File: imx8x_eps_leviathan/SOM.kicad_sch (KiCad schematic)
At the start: 2 parts, among them J10 BTH-070-02-L-D-A, J9 BTH-070-02-L-D-A (A to B)

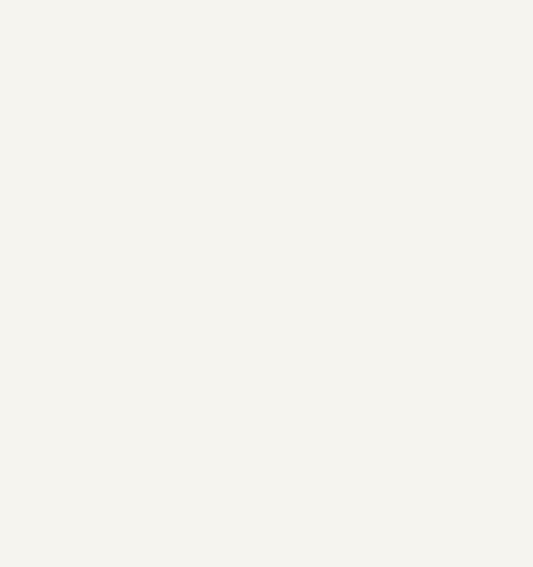
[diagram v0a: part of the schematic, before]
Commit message: WIP Ethernet
Don't have right lib on my laptop
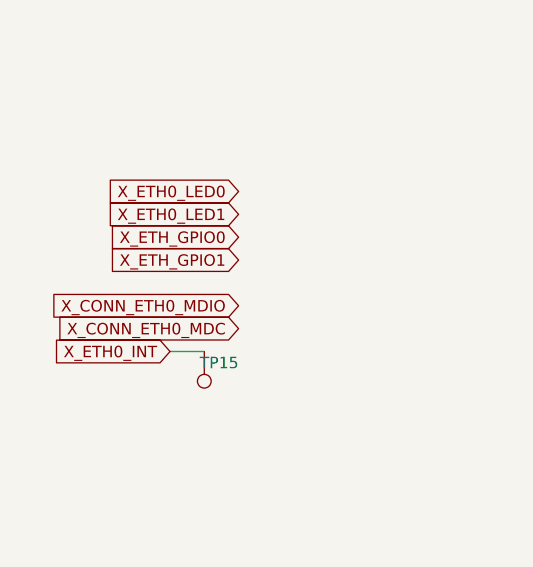
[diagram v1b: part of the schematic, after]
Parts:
- added TP15: TestPoint, TestPoint:TestPoint_THTPad_1.0x1.0mm_Drill0.5mm, symbol Connector:TestPoint
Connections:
- new net X_ETH0_INT: TP15.1
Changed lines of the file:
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@@
 		(comment 1 "By John Pollak & Luca Lanzillotta")
+	)
+	(wire
+		(pts
+			(xy 54.61 193.04) (xy 58.42 193.04)
+		)
+		(stroke
+			(width 0)
+			(type default)
+		)
+	)
+	(global_label "X_ETH0_LED1"
+		(shape input)
+		(at 62.23 177.8 180)
+		(fields_autoplaced yes)
+		(effects
+			(font
+				(size 1.27 1.27)
+			)
+			(justify right)
+		)
+		(property "Intersheetrefs" "${INTERSHEET_REFS}"
+			(at 46.7869 177.8 0)
+			(effects
+				(font
+					(size 1.27 1.27)
+				)
+				(justify right)
+				(hide yes)
+			)
+		)
+	)
+	(global_label "X_ETH0_LED0"
+		(shape input)
+		(at 62.23 175.26 180)
+		(fields_autoplaced yes)
+		(effects
+			(font
+				(size 1.27 1.27)
+			)
+			(justify right)
+		)
+		(property "Intersheetrefs" "${INTERSHEET_REFS}"
+			(at 46.7869 175.26 0)
+			(effects
+				(font
+					(size 1.27 1.27)
+				)
+				(justify right)
+				(hide yes)
+			)
+		)
+	)
+	(global_label "X_ETH_GPIO1"
+		(shape input)
+		(at 62.23 182.88 180)
+		(fields_autoplaced yes)
+		(effects
+			(font
+				(size 1.27 1.27)
+			)
+			(justify right)
+		)
+		(property "Intersheetrefs" "${INTERSHEET_REFS}"
+			(at 46.9682 182.88 0)
+			(effects
+				(font
+					(size 1.27 1.27)
+				)
+				(justify right)
+				(hide yes)
+			)
+		)
+	)
+	(global_label "X_CONN_ETH0_MDIO"
+		(shape input)
+		(at 62.23 187.96 180)
+		(fields_autoplaced yes)
+		(effects
+			(font
+				(size 1.27 1.27)
+			)
+			(justify right)
+		)
+		(property "Intersheetrefs" "${INTERSHEET_REFS}"
+			(at 40.5577 187.96 0)
+			(effects
+				(font
+					(size 1.27 1.27)
+				)
+				(justify right)
+				(hide yes)
+			)
+		)
+	)
+	(global_label "X_CONN_ETH0_MDC"
+		(shape input)
+		(at 62.23 190.5 180)
+		(fields_autoplaced yes)
+		(effects
+			(font
+				(size 1.27 1.27)
+			)
+			(justify right)
+		)
+		(property "Intersheetrefs" "${INTERSHEET_REFS}"
+			(at 41.223 190.5 0)
+			(effects
+				(font
+					(size 1.27 1.27)
+				)
+				(justify right)
+				(hide yes)
+			)
+		)
+	)
+	(global_label "X_ETH0_INT"
+		(shape input)
+		(at 54.61 193.04 180)
+		(fields_autoplaced yes)
+		(effects
+			(font
+				(size 1.27 1.27)
+			)
+			(justify right)
+		)
+		(property "Intersheetrefs" "${INTERSHEET_REFS}"
+			(at 40.9206 193.04 0)
+			(effects
+				(font
+					(size 1.27 1.27)
+				)
+				(justify right)
+				(hide yes)
+			)
+		)
+	)
+	(global_label "X_ETH_GPIO0"
+		(shape input)
+		(at 62.23 180.34 180)
+		(fields_autoplaced yes)
+		(effects
+			(font
+				(size 1.27 1.27)
+			)
+			(justify right)
+		)
+		(property "Intersheetrefs" "${INTERSHEET_REFS}"
+			(at 46.9682 180.34 0)
+			(effects
+				(font
+					(size 1.27 1.27)
+				)
+				(justify right)
+				(hide yes)
+			)
+		)
 	)
 	(symbol
@@
 					(unit 1)
 				)
+			)
+		)
+	)
+	(symbol
+		(lib_id "Connector:TestPoint")
+		(at 58.42 193.04 180)
+		(unit 1)
+		(exclude_from_sim no)
+		(in_bom yes)
+		(on_board yes)
+		(dnp no)
+		(property "Reference" "TP15"
+			(at 62.23 194.31 0)
+			(effects
+				(font
+					(size 1.27 1.27)
+				)
+				(justify left)
+			)
+		)
+		(property "Value" "TestPoint"
+			(at 58.166 194.056 0)
+			(effects
+				(font
+					(size 1.27 1.27)
+				)
+				(justify left)
+				(hide yes)
+			)
+		)
+		(property "Footprint" "TestPoint:TestPoint_THTPad_1.0x1.0mm_Drill0.5mm"
+			(at 53.34 193.04 0)
+			(effects
+				(font
+					(size 1.27 1.27)
+				)
+				(hide yes)
+			)
+		)
+		(property "Datasheet" "~"
+			(at 53.34 193.04 0)
+			(effects
+				(font
+					(size 1.27 1.27)
+				)
+				(hide yes)
+			)
+		)
+		(property "Description" "test point"
+			(at 58.42 193.04 0)
+			(effects
+				(font
+					(size 1.27 1.27)
+				)
+				(hide yes)
+			)
+		)
+		(property "LCSC" ""
+			(at 58.42 193.04 0)
+			(effects
+				(font
+					(size 1.27 1.27)
+				)
+			)
+		)
+		(property "Voltage" ""
+			(at 58.42 193.04 0)
+			(effects
+				(font
+					(size 1.27 1.27)
+				)
+			)
+		)
+		(pin "1"
+		)
+		(instances
+			(project "imx8x_eps_leviathan"
+				(path "/bd3af9f3-19df-4a2f-8b54-98c48cea082e/1b5b2e76-614d-4307-9232-e06f7c77302d/d76dd75e-585c-4f61-92c5-bda4099b5574"
+					(reference "TP15")
+					(unit 1)
+				)

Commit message: good stufff
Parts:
- removed TP15: TestPoint, TestPoint:TestPoint_THTPad_1.0x1.0mm_Drill0.5mm, symbol Connector:TestPoint
- added C120, C121: 22uF, Capacitor_SMD:C_0603_1608Metric, symbol Device:C_Small
- added C122, C123: 4.7uF, Capacitor_SMD:C_0603_1608Metric, symbol Device:C_Small
- added C124: 100nF, Capacitor_SMD:C_0603_1608Metric, symbol Device:C_Small
- added C125: 220nF, Capacitor_SMD:C_0603_1608Metric, symbol Device:C_Small
- added R190, R191, R192, R193, R194, R195: 22, Resistor_SMD:R_0402_1005Metric, symbol Device:R_US
- added R196, R197, R198, R199, R200, R201, R202, R203, R204, R205, R206, R207, R208, R209, R210: 10k, Resistor_SMD:R_0402_1005Metric, symbol Device:R_US
- added TP16, TP17, TP47, TP48, TP49: TestPoint, TestPoint:TestPoint_THTPad_1.0x1.0mm_Drill0.5mm, symbol Connector:TestPoint
- J9: value BTH-070-02-L-D-A (A to B) -> BTH-070-02-L-D-A
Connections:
- net GND: now also J10.09 (C5), J10.10 (D5), J10.100 (D50), J10.107 (C54), J10.112 (D56), J10.115 (C58), J10.120 (D60), J10.125 (C63), J10.130 (D65), J10.19 (C10), J10.22 (D11), J10.29 (C15), J10.36 (D18), J10.39 (C20), J10.46 (D23), J10.49 (C25), J10.56 (D28), J10.59 (C30), J10.62 (D31), J10.69 (C35), J10.70 (D35), J10.79 (C40), J10.80 (D40), J10.89 (C45), J10.90 (D45), J10.95 (C48), J9.03 (A2), J9.06 (B3), J9.09 (A5), J9.100 (B50), J9.103 (A52), J9.108 (B54), J9.111 (A56), J9.12 (B6), J9.120 (B60), J9.121 (A61), J9.126 (B63), J9.13 (A7), J9.131 (A66), J9.139 (A70), J9.140 (B70), J9.18 (B9), J9.23 (A12), J9.24 (B12), J9.30 (B15), J9.36 (B18), J9.39 (A20), J9.40 (B20), J9.46 (B23), J9.49 (A25), J9.52 (B26), J9.58 (B29), J9.61 (A31), J9.64 (B32), J9.71 (A36), J9.74 (B37), J9.79 (A40), J9.80 (B40), J9.89 (A45), J9.90 (B45), C120.2, C121.2, C122.2, C123.2, C124.2, C125.2, R196.1, R197.1, R198.1, R199.1, R200.1, R201.1, R202.1, R203.1, R204.1, R205.1, R206.1, R207.1, R208.1, R209.1, R210.1
- net VCC_1V8_OUT: now also J10.127 (C64), TP47.1
- net VCC_3V3_OUT: now also J10.129 (C65), TP17.1
- net VCC_LDO_SD1: now also J9.33 (A17)
- net VCC_SCU_1V8: now also J10.93 (C47)
- net VDD_ADC_1V8: now also J10.114 (D57), C125.1
- net X_CONN_ETH0_MDC: now also J9.135 (A68)
- net X_CONN_ETH0_MDIO: now also J9.133 (A67)
- net X_ETH0_INT: now also J9.137 (A69), TP16.1
- net X_ETH0_LED0: now also J9.123 (A62)
- net X_ETH0_LED1: now also J9.125 (A63)
- net X_ETH_GPIO0: now also J9.127 (A64)
- net X_ETH_GPIO1: now also J9.129 (A65)
- net X_POR_B_1V8: now reaches J10.101 (C51)
- net X_POR_B_3V3: now reaches J10.103 (C52)
- net X_POR_B_3V3: now also TP49.1
- net X_PGOOD: now reaches J10.105 (C53)
- net X_PMIC_EWARN: now reaches J10.109 (C55)
- net X_LSIO_QSPIOB_SS0_B: now reaches J10.11 (C6)
- net X_SCU_PMIC_ON_REQ: now reaches J10.111 (C56)
- net X_SCU_PMIC_STANDBY: now reaches J10.113 (C57)
- net X_LSIO_GPIO1_IO09: now reaches J10.116 (D58)
- net X_PMIC_INT_B: now reaches J10.117 (C59)
- net X_LSIO_GPIO1_IO10: now reaches J10.118 (D59)
- net X_PMIC_WDI: now reaches J10.119 (C60)
- net X_LSIO_QSPI0B_DATA0: now reaches J10.12 (D6)
- net X_M40_UART0_RX: now reaches J10.121 (C61)
- net X_LSIO_GPIO1_IO14: now reaches J10.122 (D61)
- net X_SCU_WDOG0_WDOG_OUT: now reaches J10.123 (C62)
- net X_SCU_WDOG0_WDOG_OUT: now also TP48.1
- net X_M40_UART0_TX: now reaches J10.124 (D62)
- net X_LSIO_GPIO1_IO12: now reaches J10.126 (D63)
- net X_LSIO_GPIO1_IO13: now reaches J10.128 (D64)
- net X_LSIO_QSPIOB_SS1_B: now reaches J10.13 (C7)
- net +3.3V_OBC: now reaches J10.132 (D66)
- net +3.3V_OBC: now also J10.133 (C67), J10.134 (D67), J10.135 (C68), J10.136 (D68), J10.137 (C69), J10.138 (D69), J10.139 (C70), J10.140 (D70), C120.1, C121.1, C122.1, C123.1, C124.1
- net X_LSIO_QSPI0B_DATA1: now reaches J10.14 (D7)
- net X_LSIO_QSPI0B_SCLK: now reaches J10.15 (C8)
- net X_LSIO_QSPI0B_DATA2: now reaches J10.16 (D8)
- net X_LSIO_QSPI0B_DQS: now reaches J10.17 (C9)
- net X_LSIO_QSPI0B_DATA3: now reaches J10.18 (D9)
- net VCC_QSPI_1V8: now reaches J10.20 (D10)
- net X_LSIO_GPIO1_IO26: now reaches J10.21 (C11)
- net X_LSIO_GPIO1_IO25: now reaches J10.23 (C12)
- net at J10.31 (C16): now also J10.33 (C17), J10.35 (C18), J10.37 (C19), R202.2
- net at J10.41 (C21): now also J10.43 (C22), J10.45 (C23), J10.47 (C24), R203.2
- net at J10.51 (C26): now also J10.53 (C27), J10.55 (C28), J10.57 (C29), R204.2
- net at J10.61 (C31): now also J10.63 (C32), J10.65 (C33), J10.67 (C34), R205.2
- net at J10.64 (D32): now also R210.2
- net X_ADMA_I2C0_SCL: now reaches J10.66 (D33)
- net X_ADMA_I2C0_SDA: now reaches J10.68 (D34)
- net at J10.71 (C36): now also J10.73 (C37), J10.75 (C38), J10.77 (C39), R206.2
- net at J10.76 (D38): now also J10.78 (D39), R207.2
- net X_LSIO_GPIO1_IO29: now reaches J10.81 (C41)
- net at J10.82 (D41): now also J10.84 (D42), J10.86 (D43), J10.88 (D44), R208.2
- net X_LSIO_GPIO1_IO30: now reaches J10.83 (C42)
- net ~{X_nRESET_IN}: now reaches J10.91 (C46)
- net at J10.92 (D46): now also J10.94 (D47), J10.96 (D48), J10.98 (D49), R209.2
- net at J9.02 (B1): now also R198.2
- net at J9.04 (B2): now also R199.2
- net at J9.08 (B4): now also R200.2
- net at J9.10 (B5): now also R201.2
- net X_ADMA_UART2_TX: now reaches J9.101 (A51)
- net X_CONN_ENET1_RXD0: now reaches J9.102 (B51)
- net X_CONN_ENET1_RX_CTL: now reaches J9.104 (B52)
- net X_CONN_ENET1_REFCLK: now reaches J9.106 (B53)
- net X_ADMA_I2C3_SDA: now reaches J9.107 (A54)
- net X_ADMA_I2C3_SCL: now reaches J9.112 (B56)
- net X_ETH0_D_RXDV_N: now reaches J9.122 (B61)
- net X_ETH0_D_RXDV_P: now reaches J9.124 (B62)
- net X_ETH0_C_TXCLK_N: now reaches J9.128 (B64)
- net X_ETH0_C_TXCLK_P: now reaches J9.130 (B65)
- net X_ETH0_B_TX_N: now reaches J9.132 (B66)
- net X_ETH0_B_TX_P: now reaches J9.134 (B67)
- net X_ETH0_A_TX_N: now reaches J9.136 (B68)
- net X_ETH0_A_TX_P: now reaches J9.138 (B69)
- net X_CONN_USDHC1_VSELECT: now reaches J9.15 (A8)
- net X_CONN_USDHC1_CD_B: now reaches J9.19 (A10)
- net X_CONN_USDHC1_RESET_B: now reaches J9.21 (A11)
- net at J9.25 (A13): now also R190.2
- net at J9.26 (B13): now also J9.28 (B14), R196.2
- net at J9.27 (A14): now also R191.2
- net at J9.29 (A15): now also R192.2
- net at J9.31 (A16): now also R193.2
- net at J9.32 (B16): now also J9.34 (B17), R197.2
- net at J9.35 (A18): now also R194.2
- net at J9.37 (A19): now also R195.2
- net X_ADMA_SPI2_CS0: now reaches J9.41 (A21)
- net X_ADMA_SPI2_SCK: now reaches J9.43 (A22)
- net X_ADMA_SPI2_SDI: now reaches J9.45 (A23)
- net X_ADMA_SPI2_SDO: now reaches J9.47 (A24)
- net X_BOOT_MODE0: now reaches J9.66 (B33)
- net X_ADMA_SPI2_CS1: now reaches J9.67 (A34)
- net X_BOOT_MODE1: now reaches J9.68 (B34)
- net X_BOOT_MODE2: now reaches J9.70 (B35)
- net X_BOOT_MODE3: now reaches J9.72 (B36)
- net X_CONN_ENET1_TXD2: now reaches J9.76 (B38)
- net X_CONN_ENET1_TXC: now reaches J9.78 (B39)
- net X_CONN_ENET1_TXD3: now reaches J9.82 (B41)
- net X_CONN_ENET1_TX_CTL: now reaches J9.84 (B42)
- net X_LSO_GPIO1_IO17: now reaches J9.85 (A43)
- net X_CONN_ENET1_RXC: now reaches J9.86 (B43)
- net X_LSO_GPIO1_IO18: now reaches J9.87 (A44)
- net X_CONN_ENET1_RXD3: now reaches J9.88 (B44)
- net X_LSO_GPIO1_IO20: now reaches J9.91 (A46)
- net X_CONN_ENET1_RXD2: now reaches J9.92 (B46)
- net X_LSO_GPIO1_IO19: now reaches J9.93 (A47)
- net X_CONN_ENET1_RXD1: now reaches J9.94 (B47)
- net X_ADMA_UART0_TX: now reaches J9.95 (A48)
- net X_CONN_ENET1_TXD0: now reaches J9.96 (B48)
- net X_ADMA_UART0_RX: now reaches J9.97 (A49)
- net X_CONN_ENET1_TXD1: now reaches J9.98 (B49)
- net X_ADMA_UART2_RX: now reaches J9.99 (A50)
- new net X_CONN_USDHC1_CLK: R194.1
- new net X_CONN_USDHC1_CMD: R195.1
- new net X_CONN_USDHC1_DATA0: R193.1
- new net X_CONN_USDHC1_DATA1: R192.1
- new net X_CONN_USDHC1_DATA2: R191.1
- new net X_CONN_USDHC1_DATA3: R190.1
- no-connect marks 0 -> 85
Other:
- note added: "Switch the watchdog and the m40 uart"

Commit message: bruh
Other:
- title: (none) -> Leviathan 1-A
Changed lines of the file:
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@@
 	(paper "A3")
 	(title_block
+		(title "Leviathan 1-A")
+		(date "2025-10-22")
+		(rev "1-A")
 		(company "Bronco Space Lab")
 		(comment 1 "By John Pollak & Luca Lanzillotta")

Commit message: Updated Schematic and SOM
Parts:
- removed TP48: TestPoint, TestPoint:TestPoint_THTPad_1.0x1.0mm_Drill0.5mm, symbol Connector:TestPoint
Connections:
- net X_LSIO_GPIO1_IO12 renamed X_CONN_ETH1_PHY_INT
- net X_SCU_WDOG0_WDOG_OUT: no longer names the net of J10.123 (C62)
- no-connect marks 85 -> 86
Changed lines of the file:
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@@
 	)
 	(junction
-		(at 258.572 195.072)
-		(diameter 0)
-		(color 0 0 0 0)
-	)
-	(junction
 		(at 292.862 212.852)
 		(diameter 0)
@@
 	)
 	(no_connect
+		(at 266.192 195.072)
+	)
+	(no_connect
 		(at 291.592 167.132)
 	)
@@
 	(wire
 		(pts
-			(xy 278.892 226.314) (xy 278.892 231.902)
+			(xy 278.892 228.346) (xy 278.892 231.902)
 		)
 		(stroke
@@
 	(wire
 		(pts
-			(xy 257.302 195.072) (xy 258.572 195.072)
-		)
-		(stroke
-			(width 0)
-			(type default)
-		)
-	)
-	(wire
-		(pts
 			(xy 120.142 115.062) (xy 120.142 127.762)
 		)
@@
 	(wire
 		(pts
-			(xy 258.572 195.072) (xy 266.192 195.072)
-		)
-		(stroke
-			(width 0)
-			(type default)
-		)
-	)
-	(wire
-		(pts
 			(xy 261.112 182.372) (xy 266.192 182.372)
 		)
@@
 		)
 	)
-	(global_label "X_LSIO_GPIO1_IO12"
-		(shape bidirectional)
-		(at 296.672 197.612 0)
-		(fields_autoplaced yes)
-		(effects
-			(font
-				(size 1.27 1.27)
-			)
-			(justify left)
-		)
-		(property "Intersheetrefs" "${INTERSHEET_REFS}"
-			(at 319.0928 197.612 0)
-			(effects
-				(font
-					(size 1.27 1.27)
-				)
-				(justify left)
-				(hide yes)
-			)
-		)
-	)
 	(global_label "X_CONN_ENET1_RX_CTL"
 		(shape input)
@@
 		)
 	)
-	(global_label "+3.3V_OBC"
+	(global_label "X_CONN_ETH1_PHY_INT"
 		(shape input)
-		(at 278.892 226.314 0)
+		(at 296.672 197.612 0)
 		(fields_autoplaced yes)
 		(effects
@@
 		)
 		(property "Intersheetrefs" "${INTERSHEET_REFS}"
-			(at 292.4001 226.314 0)
+			(at 321.2472 197.612 0)
 			(effects
 				(font
@@
 		)
 	)
-	(global_label "X_SCU_WDOG0_WDOG_OUT"
-		(shape input)
-		(at 257.302 195.072 180)
-		(fields_autoplaced yes)
-		(effects
-			(font
-				(size 1.27 1.27)
-			)
-			(justify right)
-		)
-		(property "Intersheetrefs" "${INTERSHEET_REFS}"
-			(at 229.945 195.072 0)
-			(effects
-				(font
-					(size 1.27 1.27)
-				)
-				(justify right)
-				(hide yes)
-			)
-		)
-	)
 	(global_label "X_BOOT_MODE1"
 		(shape input)
@@
 	)
 	(symbol
-		(lib_id "Connector:TestPoint")
-		(at 258.572 195.072 180)
-		(unit 1)
-		(exclude_from_sim no)
-		(in_bom yes)
-		(on_board yes)
-		(dnp no)
-		(property "Reference" "TP48"
-			(at 259.842 198.247 0)
-			(effects
-				(font
-					(size 1.27 1.27)
-				)
-				(justify right)
-			)
-		)
-		(property "Value" "TestPoint"
-			(at 261.112 199.6439 0)
-			(effects
-				(font
-					(size 1.27 1.27)
-				)
-				(justify right)
-				(hide yes)
-			)
-		)
-		(property "Footprint" "TestPoint:TestPoint_THTPad_1.0x1.0mm_Drill0.5mm"
-			(at 253.492 195.072 0)
-			(effects
-				(font
-					(size 1.27 1.27)
-				)
-				(hide yes)
-			)
-		)
-		(property "Datasheet" "~"
-			(at 253.492 195.072 0)
-			(effects
-				(font
-					(size 1.27 1.27)
-				)
-				(hide yes)
-			)
-		)
-		(property "Description" "test point"
-			(at 258.572 195.072 0)
-			(effects
-				(font
-					(size 1.27 1.27)
-				)
-				(hide yes)
-			)
-		)
-		(property "LCSC" ""
-			(at 258.572 195.072 0)
-			(effects
-				(font
-					(size 1.27 1.27)
-				)
-			)
-		)
-		(property "Voltage" ""
-			(at 258.572 195.072 0)
-			(effects
-				(font
-					(size 1.27 1.27)
-				)
-			)
-		)
-		(pin "1"
-		)
-		(instances
-			(project "imx8x_eps_leviathan"
-				(path "/bd3af9f3-19df-4a2f-8b54-98c48cea082e/1b5b2e76-614d-4307-9232-e06f7c77302d/d76dd75e-585c-4f61-92c5-bda4099b5574"
-					(reference "TP48")
-					(unit 1)
-				)
-			)
-		)
-	)
-	(symbol
 		(lib_id "Device:R_US")
 		(at 112.522 74.422 90)
@@
 		(dnp no)
 		(property "Reference" "TP16"
-			(at 117.602 212.852 0)
+			(at 118.872 213.106 0)
 			(effects
 				(font
@@
 					(unit 1)
 				)
+			)
+		)
+	)
+	(symbol
+		(lib_id "power:+3.3V")
+		(at 278.892 228.346 0)
+		(unit 1)
+		(exclude_from_sim no)
+		(in_bom yes)
+		(on_board yes)
+		(dnp no)
+		(property "Reference" "#PWR0170"
+			(at 278.892 232.156 0)
+			(effects
+				(font
+					(size 1.27 1.27)
+				)
+				(hide yes)
+			)
+		)
+		(property "Value" "+3.3V_OBC"
+			(at 284.226 224.79 0)
+			(effects
+				(font
+					(size 1.27 1.27)
+				)
+			)
+		)
+		(property "Footprint" ""
+			(at 278.892 228.346 0)
+			(effects
+				(font
+					(size 1.27 1.27)
+				)
+				(hide yes)
+			)
+		)
+		(property "Datasheet" ""
+			(at 278.892 228.346 0)
+			(effects
+				(font
+					(size 1.27 1.27)
+				)
+				(hide yes)
+			)
+		)
+		(property "Description" "Power symbol creates a global label with name \"+3.3V\""
+			(at 278.892 228.346 0)
+			(effects
+				(font
+					(size 1.27 1.27)
+				)
+				(hide yes)
+			)
+		)
+		(pin "1"
+		)
+		(instances
+			(project "imx8x_eps_leviathan"
+				(path "/bd3af9f3-19df-4a2f-8b54-98c48cea082e/1b5b2e76-614d-4307-9232-e06f7c77302d/d76dd75e-585c-4f61-92c5-bda4099b5574"
+					(reference "#PWR0170")
+					(unit 1)
+				)
